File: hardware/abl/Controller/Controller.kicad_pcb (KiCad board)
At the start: 4 copper layers, 56.2 x 74 mm, 23 parts, among them IC1 LSF0204PWJ, IC3 VEML6040A3OG, IC4 FXL6408UMX, J1 SFW20S-2STE1LF, J2 Conn_02x03_Odd_Even, J3 Conn_02x03_Odd_Even, J4 PRT-14417, J5 Conn_02x04_Odd_Even, U1 INA219AxD

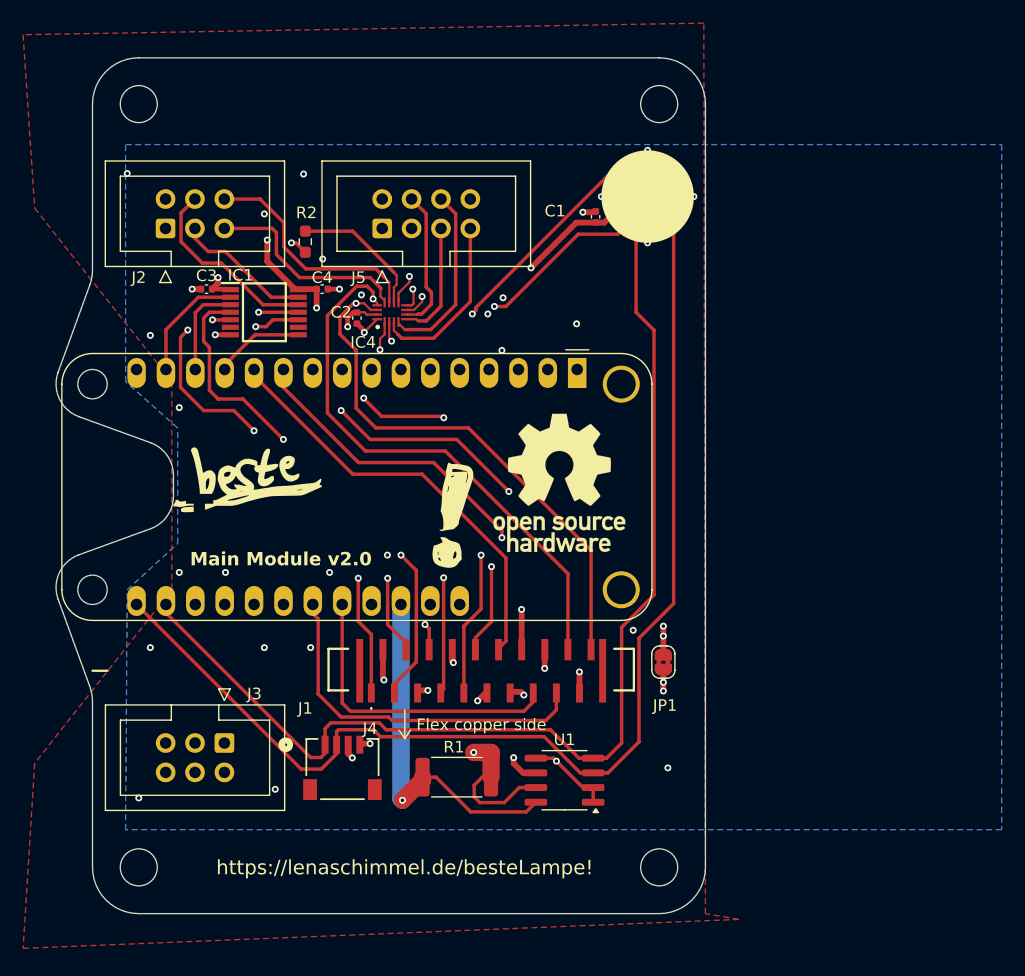
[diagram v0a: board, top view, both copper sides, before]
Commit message: Clean up schematics and minor fixes in PCB layouts.
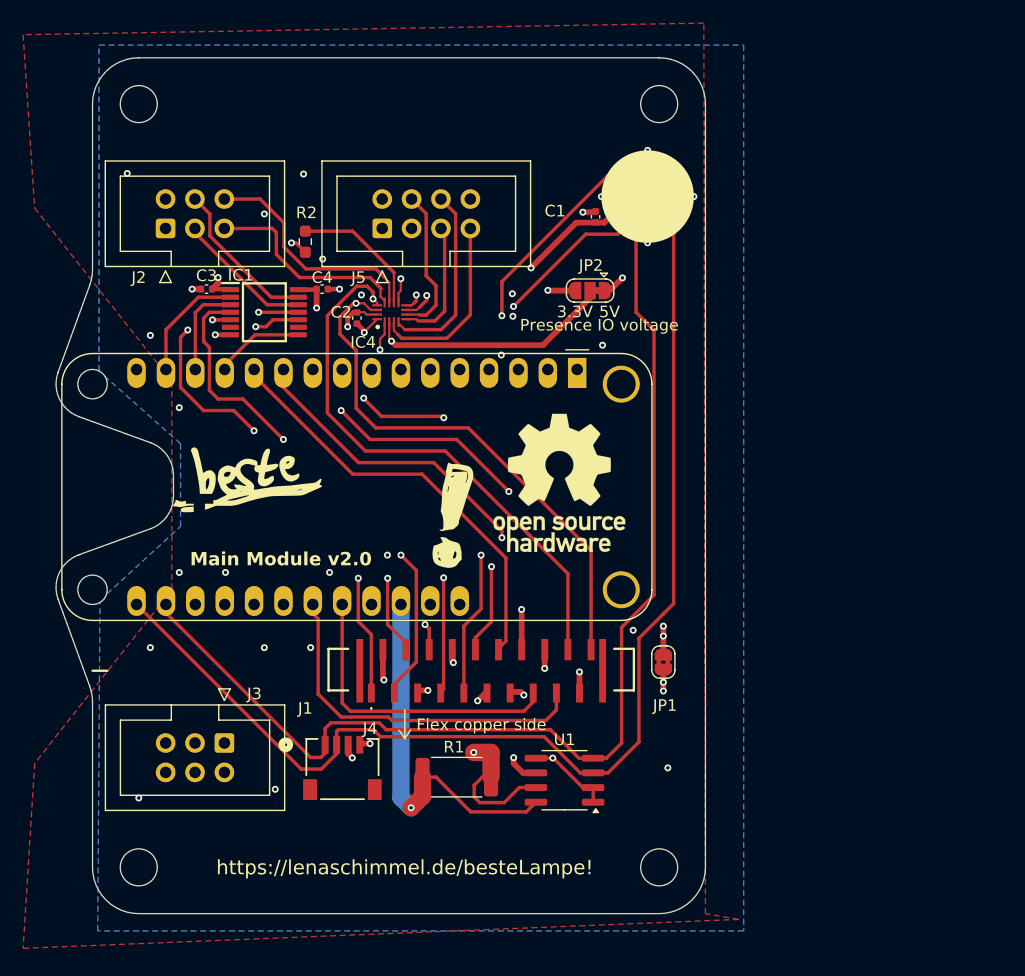
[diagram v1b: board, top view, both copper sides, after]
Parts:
- added JP2: SolderJumper_3_Bridged12, Jumper:SolderJumper-3_P1.3mm_Bridged12_RoundedPad1.0x1.5mm, F.Cu at (106.0, 71.1)
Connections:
- net Net-(A1-USB) renamed VBUS
- net Net-(IC4-GPIO0) renamed /S1_L
- net Net-(IC4-GPIO1) renamed /S2_L
- net Net-(IC4-GPIO2) renamed /S1_R
- net Net-(IC4-GPIO3) renamed /S2_R
- net Net-(IC4-GPIO4) renamed /FX4
- net Net-(IC4-GPIO5) renamed /FX5
- net Net-(IC4-GPIO6) renamed /FX6
- net Net-(IC4-GPIO7) renamed /FX7
- C4 pad 2: +5V -> Net-(IC1-REFB)
- IC1 pad 10: Net-(IC1-B4) -> /RX_R_5
- IC1 pad 11: Net-(IC1-B3) -> /TX_R_5
- IC1 pad 12: Net-(IC1-B2) -> /RX_L_5
- IC1 pad 13: Net-(IC1-B1) -> /TX_L_5
- IC1 pad 14: +5V -> Net-(IC1-REFB)
- IC4 pad 2: +5V -> Net-(IC1-REFB)
- J2 pad 3: Net-(IC1-B1) -> /RX_L_5
- J2 pad 4: Net-(IC1-B2) -> /TX_L_5
- J3 pad 3: Net-(IC1-B3) -> /RX_R_5
- J3 pad 4: Net-(IC1-B4) -> /TX_R_5
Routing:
- net Net-(IC1-B4): track 48.7 -> 0.00 mm, vias 1 -> 0
- net /TX_R_5: track 0.00 -> 48.5 mm, vias 0 -> 1
- net /RX_R_5: track 0.00 -> 46.2 mm, vias 0 -> 1
- net Net-(IC1-B3): track 44.7 -> 0.00 mm, vias 1 -> 0
- net Net-(IC1-REFB): track 0.00 -> 32.4 mm, vias 0 -> 2
- net +5V: track 168.3 -> 150.2 mm, vias 6 -> 4
- net Net-(IC1-B2): track 16.6 -> 0.00 mm
- net /TX_L_5: track 0.00 -> 13.6 mm
- net Net-(IC1-B1): track 11.9 -> 0.00 mm
- net /RX_L_5: track 0.00 -> 11.9 mm
- net /S2_R: track 61.8 -> 66.1 mm
- net /SDA: track 184.0 -> 185.6 mm
- net VBUS: track 31.1 -> 32.4 mm
- net /FX5: track 10.3 -> 11.0 mm
- net /FX7: track 15.3 -> 15.9 mm
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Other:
- board text added: "3.3V"
- board text added: "5V"
- board text added: "Presence IO voltage"

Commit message: Improved connectors (more signals, better return paths)
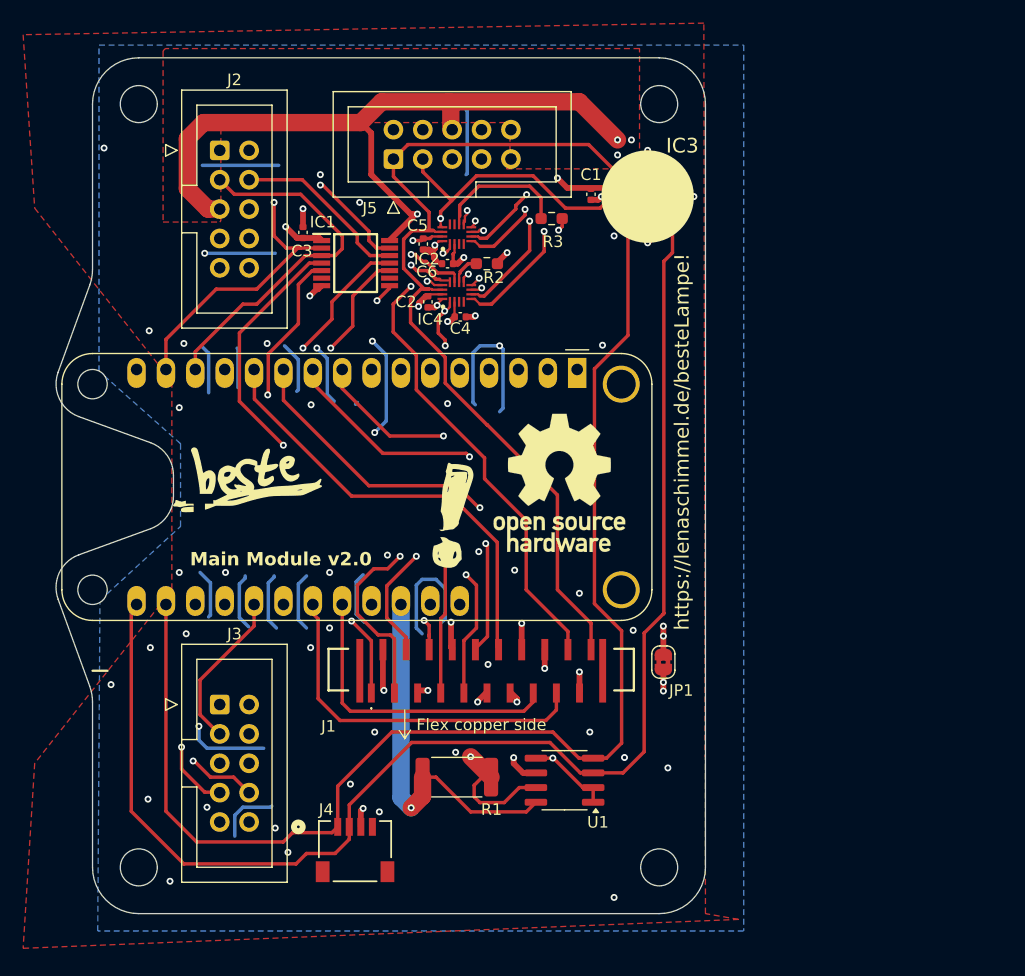
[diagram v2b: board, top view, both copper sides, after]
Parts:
- removed JP2: SolderJumper_3_Bridged12, Jumper:SolderJumper-3_P1.3mm_Bridged12_RoundedPad1.0x1.5mm
- added C5: 100nF, Capacitor_SMD:C_0402_1005Metric, F.Cu at (91.6, 67.1)
- added C6: 100nF, Capacitor_SMD:C_0402_1005Metric, F.Cu at (93.7, 68.8)
- added IC2: FXL6408UMX, FXL6408UMX:QFN40P180X260X55-16N, F.Cu at (94.5, 66.2)
- added R3: 4700R, Resistor_SMD:R_0603_1608Metric_Pad0.98x0.95mm_HandSolder, F.Cu at (102.7, 64.9)
- J2, J3: footprint Connector_IDC:IDC-Header_2x03_P2.54mm_Vertical -> Connector_IDC:IDC-Header_2x05_P2.54mm_Vertical
- J5: footprint Connector_IDC:IDC-Header_2x04_P2.54mm_Vertical -> Connector_IDC:IDC-Header_2x05_P2.54mm_Vertical
- moved R2 15.8 mm to (97.1, 68.8), turned to 0 degrees
- moved C4 12.2 mm to (94.8, 73.4)
- moved C3 9.67 mm to (81.2, 66.1), turned to -90 degrees
- moved IC1 8.96 mm to (85.8, 68.8)
- moved J2 8.22 mm to (74.0, 59.0), turned to 0 degrees
- moved J4 7.18 mm to (85.7, 119.6)
- moved C2 6.30 mm to (92.0, 72.1)
- moved J5 6.08 mm to (89.0, 59.8)
- moved IC4 5.91 mm to (94.5, 71.2)
- moved J3 3.35 mm to (74.0, 106.9), turned to 0 degrees
- moved C1 1.99 mm to (106.1, 62.8), turned to -90 degrees
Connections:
- net /FX5 renamed /FX_3_5
- C4 pad 2: Net-(IC1-REFB) -> +3.3V
- IC1 pad 14: Net-(IC1-REFB) -> +5V
- IC4 pad 11: /S2_L -> /FX_3_1
- IC4 pad 12: /S1_L -> /FX_3_0
- IC4 pad 2: Net-(IC1-REFB) -> +3.3V
- IC4 pad 3: /FX7 -> /FX_3_7
- IC4 pad 4: /FX6 -> /FX_3_6
- IC4 pad 6: /FX4 -> /FX_3_4
- IC4 pad 7: /S2_R -> /FX_3_3
- IC4 pad 8: /S1_R -> /FX_3_2
- J2 pad 1: +5V -> /TX_L
- J2 pad 3: /RX_L_5 -> /RX_L
- J2 pad 4: /TX_L_5 -> /RX_L_5
- J2 pad 5: /S1_L -> +5V
- J2 pad 6: /S2_L -> /TX_L_5
- J3 pad 1: +5V -> /TX_R
- J3 pad 3: /RX_R_5 -> /RX_R
- J3 pad 4: /TX_R_5 -> /RX_R_5
- J3 pad 5: /S1_R -> +5V
- J3 pad 6: /S2_R -> /TX_R_5
- J5 pad 1: +5V -> /SDA
- J5 pad 2: GND -> +3.3V
- J5 pad 3: +3.3V -> /SCL
- J5 pad 4: /FX4 -> +4V
- J5 pad 6: /FX6 -> +5V
- J5 pad 7: /FX7 -> /FX_5_5
- J5 pad 8: +4V -> /FX_3_4
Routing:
- net GND: track 20.0 -> 223.1 mm, vias 39 -> 59
- net /FX_3_3: track 0.00 -> 76.6 mm, vias 0 -> 2
- net /FX_3_2: track 0.00 -> 70.6 mm, vias 0 -> 2
- net /FX_5_3: track 0.00 -> 69.6 mm, vias 0 -> 1
- net /FX_5_2: track 0.00 -> 69.6 mm, vias 0 -> 1
- net /S2_R: track 66.1 -> 0.00 mm, vias 1 -> 0
- net /S1_R: track 59.1 -> 0.00 mm, vias 1 -> 0
- net +3.3V: track 155.2 -> 200.7 mm, vias 8 -> 11
- net +5V: track 150.2 -> 194.8 mm, vias 4 -> 8
- net Net-(IC1-REFB): track 32.4 -> 0.00 mm, vias 2 -> 0
- net /FX_3_4: track 0.00 -> 23.4 mm, vias 0 -> 1
- net /RX_L: track 8.23 -> 31.7 mm
- net /TX_L: track 10.2 -> 32.8 mm, vias 0 -> 1
- net /FX_3_0: track 0.00 -> 21.3 mm, vias 0 -> 1
- net /SDA: track 185.6 -> 205.9 mm, vias 2 -> 0
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- added copper zone on F.Cu, net +5V
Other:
- board text removed: "3.3V"
- board text removed: "5V"
- board text removed: "Presence IO voltage"

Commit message: Improved grounding.
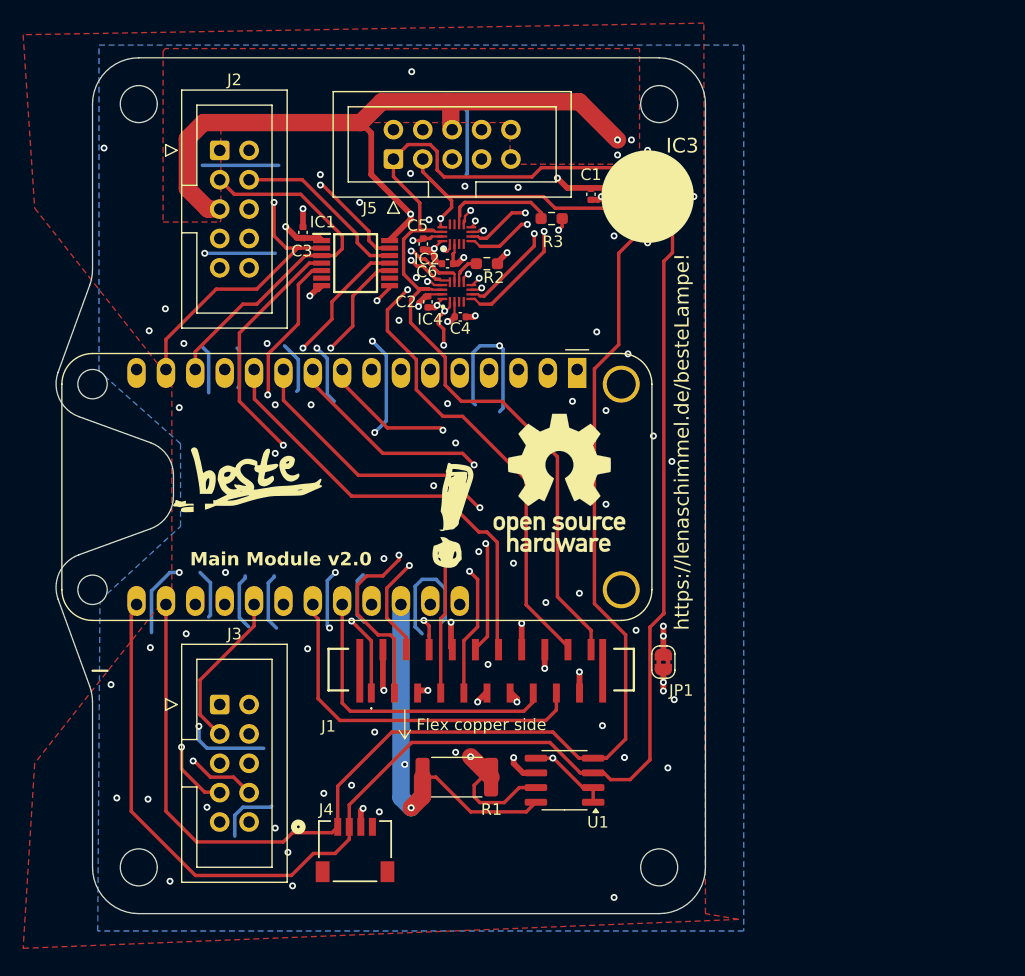
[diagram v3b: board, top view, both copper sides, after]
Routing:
- net +3.3V: track 200.7 -> 158.8 mm
- net /SDA: track 205.9 -> 212.3 mm
- net GND: track 223.1 -> 219.2 mm, vias 59 -> 83
- net /SCL: track 188.7 -> 191.3 mm
- net Net-(IC2-/RST): track 11.7 -> 9.71 mm
- net +4V: track 115.5 -> 117.2 mm
- net /FX_5_5: track 12.4 -> 13.2 mm
- net /FX_3_0: track 21.3 -> 22.0 mm
- net /FX_3_5: track 31.0 -> 31.7 mm
- net /FX_5_4: track 12.8 -> 13.5 mm
- added copper zone on In2.Cu, net GND

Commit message: Add Mosfets to power down presence sensory individually.
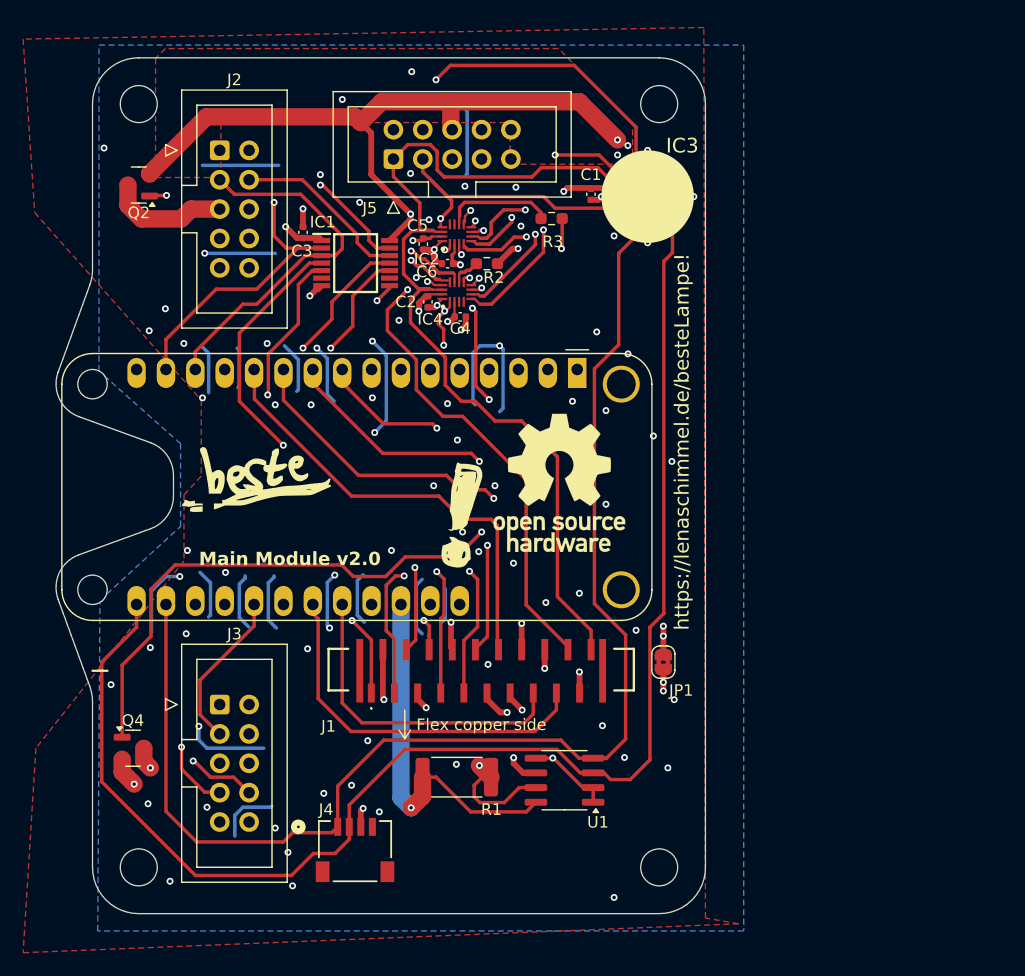
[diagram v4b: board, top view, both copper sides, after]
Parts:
- added Q2: AO3401A, Package_TO_SOT_SMD:SOT-23, F.Cu at (67.0, 62.0)
- added Q4: AO3401A, Package_TO_SOT_SMD:SOT-23, F.Cu at (66.5, 110.7)
- moved G*** 0.78 mm to (83.9, 89.8)
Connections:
- J2 pad 5: +5V -> Net-(J2-Pin_5)
- J3 pad 5: +5V -> Net-(J3-Pin_5)
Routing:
- net /FX_5_6: track 0.00 -> 77.5 mm, vias 0 -> 4
- net /FX_5_7: track 0.00 -> 72.4 mm, vias 0 -> 4
- net GND: track 219.2 -> 240.1 mm, vias 83 -> 87
- net Net-(J2-Pin_5): track 0.00 -> 10.5 mm
- net Net-(J3-Pin_5): track 0.00 -> 8.64 mm, vias 0 -> 1
- net +3.3V: track 158.8 -> 154.8 mm
- net +5V: track 194.4 -> 191.3 mm, vias 8 -> 9
- net /i3: track 32.3 -> 29.6 mm
- net /FX_5_5: track 13.2 -> 11.2 mm
- net /i7: track 36.4 -> 38.0 mm
- net /SDA: track 212.3 -> 213.9 mm
- net /EN_LED: track 26.5 -> 28.0 mm
- net /i2: track 26.5 -> 25.3 mm
- net /i8: track 39.2 -> 40.1 mm
- net /i6: track 39.7 -> 40.6 mm
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
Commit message: Minor optimizations.
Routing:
- net /i6: track 40.6 -> 39.8 mm
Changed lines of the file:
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@@
 		(tags "SOT TO_SOT_SMD")
 		(property "Reference" "Q4"
-			(at 0 -2.4 360)
+			(at 0 -2.4 0)
 			(layer "F.SilkS")
 			(effects
@@
 		)
 		(property "Value" "AO3401A"
-			(at 0 2.4 360)
+			(at 0 2.4 0)
 			(layer "F.Fab")
 			(effects
@@
 		)
 		(fp_text user "${REFERENCE}"
-			(at 0 0 360)
+			(at 0 0 0)
 			(layer "F.Fab")
 			(effects
@@
 	)
 	(segment
-		(start 88.1 85.2)
-		(end 82.05 79.15)
-		(width 0.3)
-		(layer "F.Cu")
-		(net 6)
-	)
-	(segment
-		(start 95.75 85.2)
+		(start 95.45 85.2)
 		(end 88.1 85.2)
 		(width 0.3)
@@
 	)
 	(segment
-		(start 82.05 79.15)
-		(end 82.05 77.9475)
-		(width 0.3)
-		(layer "F.Cu")
-		(net 6)
-	)
-	(segment
 		(start 95.6 95.4)
 		(end 96.3 96.1)
@@
 	)
 	(segment
-		(start 96.45 85.9)
-		(end 95.75 85.2)
+		(start 82.05 79.15)
+		(end 82.05 77.9475)
 		(width 0.3)
 		(layer "F.Cu")
@@
 		(net 6)
 	)
+	(segment
+		(start 88.1 85.2)
+		(end 82.05 79.15)
+		(width 0.3)
+		(layer "F.Cu")
+		(net 6)
+	)
 	(via
 		(at 95.6 95.4)
@@
 	)
 	(via
-		(at 96.45 85.9)
+		(at 95.45 85.2)
 		(size 0.6)
 		(drill 0.3)
@@
 	)
 	(segment
-		(start 82.05 79.05)
-		(end 82.05 77.9475)
+		(start 95.6 93)
+		(end 95.6 95.4)
 		(width 0.3)
 		(layer "In2.Cu")
@@
 	)
 	(segment
-		(start 96.45 85.9)
-		(end 95.8 86.55)
+		(start 95.8 92.8)
+		(end 95.6 93)
 		(width 0.3)
 		(layer "In2.Cu")
@@
 	)
 	(segment
-		(start 95.8 92.8)
-		(end 95.6 93)
+		(start 95.8 85.55)
+		(end 95.8 92.8)
 		(width 0.3)
 		(layer "In2.Cu")
@@
 	)
 	(segment
-		(start 95.6 93)
-		(end 95.6 95.4)
+		(start 82.05 79.05)
+		(end 82.05 77.9475)
 		(width 0.3)
 		(layer "In2.Cu")
@@
 	)
 	(segment
-		(start 95.8 86.55)
-		(end 95.8 92.8)
+		(start 95.45 85.2)
+		(end 95.8 85.55)
 		(width 0.3)
 		(layer "In2.Cu")
@@
 	)
 	(via
-		(at 78.8 85.2)
+		(at 80.5 85)
 		(size 0.6)
 		(drill 0.3)
@@
 	)
 	(via
-		(at 95 92)
+		(at 95 92.25)
 		(size 0.6)
 		(drill 0.3)
@@
 	)
 	(via
-		(at 94.55 84.05)
+		(at 94.25 83)
 		(size 0.6)
 		(drill 0.3)
@@
 	)
 	(segment
-		(start 95.45 72.2)
-		(end 95.85 72.6)
-		(width 0.2)
+		(start 94.15946 70.95946)
+		(end 94.15946 68.632026)
+		(width 0.3)
 		(layer "In2.Cu")
 		(net 37)
 	)
 	(segment
-		(start 93.9 68.962196)
-		(end 93.9 70.65)
-		(width 0.2)
+		(start 95.85 72.65)
+		(end 94.15946 70.95946)
+		(width 0.3)
 		(layer "In2.Cu")
 		(net 37)
@@
 	)
 	(segment
-		(start 95.85 72.6)
-		(end 95.85 72.65)
-		(width 0.2)
-		(layer "In2.Cu")
-		(net 37)
-	)
-	(segment
-		(start 96.65 88.15)
-		(end 96.65 92)
+		(start 94.15946 68.632026)
+		(end 94.77721 68.014276)
 		(width 0.3)
 		(layer "In2.Cu")
@@
 	)
 	(segment
-		(start 94.896995 68.014276)
-		(end 94.84792 68.014276)
-		(width 0.2)
-		(layer "In2.Cu")
-		(net 37)
-	)
-	(segment
-		(start 94.84792 68.014276)
-		(end 93.9 68.962196)
-		(width 0.2)
+		(start 94.77721 68.014276)
+		(end 94.896995 68.014276)
+		(width 0.3)
 		(layer "In2.Cu")
 		(net 37)
 	)
 	(segment
-		(start 93.9 70.65)
-		(end 95.45 72.2)
-		(width 0.2)
+		(start 96.65 88.15)
+		(end 96.65 92)
+		(width 0.3)
 		(layer "In2.Cu")
 		(net 37)
@@
 	)
 	(segment
-		(start 93.5 96.45)
-		(end 94.2 95.75)
+		(start 96.4 68.7)
+		(end 96.4 66.55)
 		(width 0.3)
 		(layer "In2.Cu")
@@
 	)
 	(segment
-		(start 92.25 100.35)
-		(end 93.5 99.1)
+		(start 98.1 73.6)
+		(end 98.1 70.4)
 		(width 0.3)
 		(layer "In2.Cu")
@@
 	)
 	(segment
-		(start 96.4 66.55)
-		(end 96.1 66.25)
+		(start 74.12 117.08)
+		(end 75.4 115.8)
 		(width 0.3)
 		(layer "In2.Cu")
@@
 	)
 	(segment
-		(start 95.9 84.8)
-		(end 95.9 75.8)
+		(start 94.2 84.3)
+		(end 95.9 82.6)
 		(width 0.3)
 		(layer "In2.Cu")
@@
 	)
 	(segment
-		(start 77.4 115.8)
-		(end 79.85 113.35)
+		(start 75.4 115.8)
+		(end 77.4 115.8)
 		(width 0.3)
 		(layer "In2.Cu")
@@
 	)
 	(segment
-		(start 98.1 73.6)
-		(end 98.1 70.4)
+		(start 96.1 66.25)
+		(end 96.1 65.1)
 		(width 0.3)
 		(layer "In2.Cu")
@@
 	)
 	(segment
-		(start 95.9 75.8)
-		(end 98.1 73.6)
+		(start 77.4 115.8)
+		(end 79.85 113.35)
 		(width 0.3)
 		(layer "In2.Cu")
@@
 	)
 	(segment
-		(start 94.2 95.75)
-		(end 94.2 86.5)
+		(start 96.4 66.55)
+		(end 96.1 66.25)
 		(width 0.3)
 		(layer "In2.Cu")
@@
 	)
 	(segment
-		(start 84.85 100.35)
-		(end 92.25 100.35)
+		(start 74 117.08)
+		(end 74.12 117.08)
 		(width 0.3)
 		(layer "In2.Cu")
@@
 	)
 	(segment
-		(start 75.4 115.8)
-		(end 77.4 115.8)
+		(start 93.5 96.45)
+		(end 94.2 95.75)
 		(width 0.3)
 		(layer "In2.Cu")
@@
 	)
 	(segment
-		(start 79.85 113.35)
-		(end 79.85 105.35)
+		(start 98.1 70.4)
+		(end 96.4 68.7)
 		(width 0.3)
 		(layer "In2.Cu")
@@
 	)
 	(segment
-		(start 96.4 68.7)
-		(end 96.4 66.55)
+		(start 79.85 105.35)
+		(end 84.85 100.35)
 		(width 0.3)
 		(layer "In2.Cu")
@@
 	)
 	(segment
-		(start 96.1 66.25)
-		(end 96.1 65.1)
+		(start 84.85 100.35)
+		(end 92.25 100.35)
 		(width 0.3)
 		(layer "In2.Cu")
@@
 	)
 	(segment
-		(start 79.85 105.35)
-		(end 84.85 100.35)
+		(start 92.25 100.35)
+		(end 93.5 99.1)
 		(width 0.3)
 		(layer "In2.Cu")
@@
 	)
 	(segment
-		(start 74.12 117.08)
-		(end 75.4 115.8)
+		(start 95.9 82.6)
+		(end 95.9 75.8)
 		(width 0.3)
 		(layer "In2.Cu")
@@
 	)
 	(segment
-		(start 98.1 70.4)
-		(end 96.4 68.7)
+		(start 95.9 75.8)
+		(end 98.1 73.6)
 		(width 0.3)
 		(layer "In2.Cu")
@@
 	)
 	(segment
-		(start 94.2 86.5)
-		(end 95.9 84.8)
+		(start 94.2 95.75)
+		(end 94.2 84.3)
 		(width 0.3)
 		(layer "In2.Cu")
@@
 	)
 	(segment
-		(start 74 117.08)
-		(end 74.12 117.08)
+		(start 79.85 113.35)
+		(end 79.85 105.35)
 		(width 0.3)
 		(layer "In2.Cu")
